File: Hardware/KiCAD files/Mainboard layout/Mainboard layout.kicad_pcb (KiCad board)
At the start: 2 copper layers, 174.5 x 169.2 mm, 67 parts, among them J1 MSD-1-A, J10 Conn_01x02, J11 Conn_01x04, J12 JST_06, J13 Conn_01x08, J17 PINHD_1x8_Male, J18 PINHD_1x8_Male, J19 PINHD_1x8_Male, J2 Screw_Terminal_2_P5.00mm, J20 PINHD_1x8_Male, J22 PINHD_1x8_Male, J23 PINHD_1x8_Male, J24 PINHD_1x8_Male, J25 Conn_01x04, J26 Conn_01x04, J27 Conn_01x04, J28 PINHD_1x8_Male, J3 Screw_Terminal_2_P3.50mm, J30 USB-A1VSB6, J31 JST_03, J34 JST_03, J35 JST_03, J36 JST_03, J37 JST_03, J38 JST_03, J4 JST_06, J5 Conn_01x04, J6 JST_06, J7 JST_06, J8 Conn_01x06, J9 Conn_01x10, Q1 BS170, Q2 2DD1664, SW8 Push_Button, SW9 Push_Button, U12 ESP32-S3-WROOM-1, U3 PCA9534PW, U5 PCA9534PW

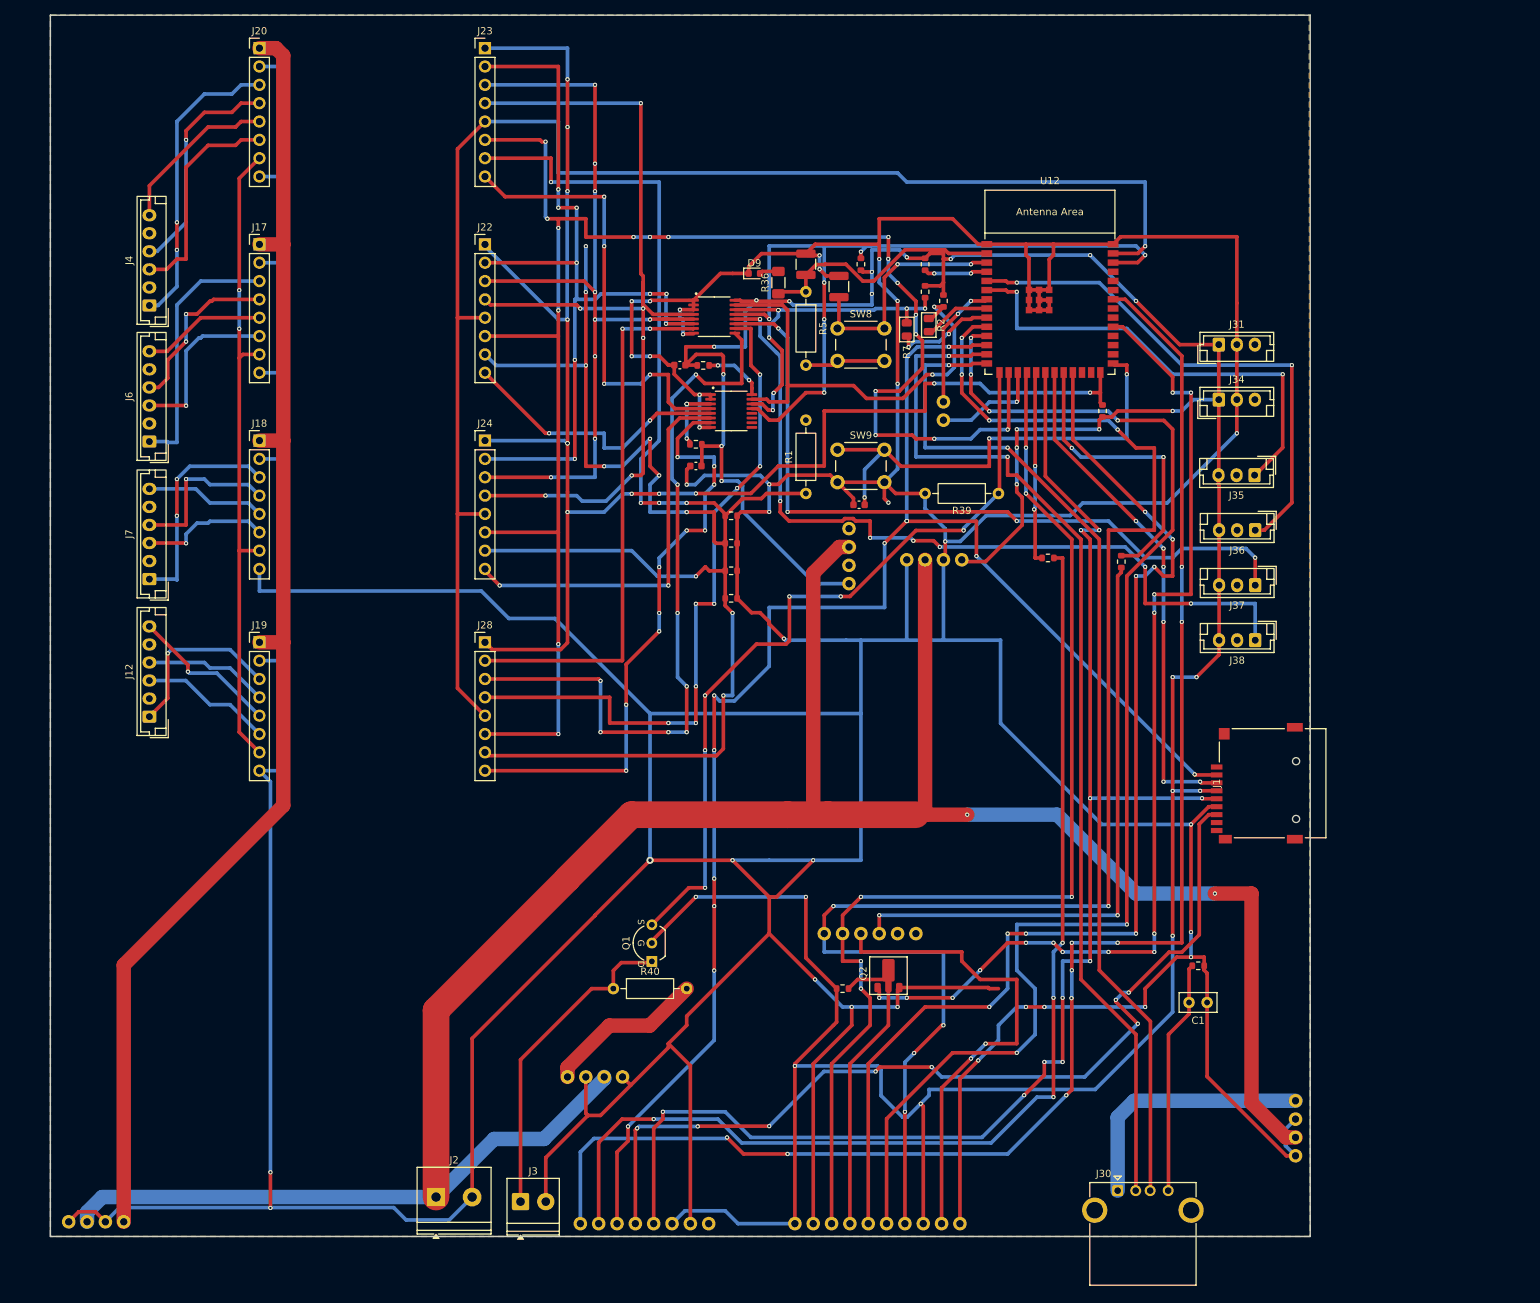
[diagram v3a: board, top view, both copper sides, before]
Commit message: general progress and adjustments
new footprint for pi reg inductor, var reg checked concurred with current part and value. re footprinted motor driver. started swapping head. adjusted some device footprints.
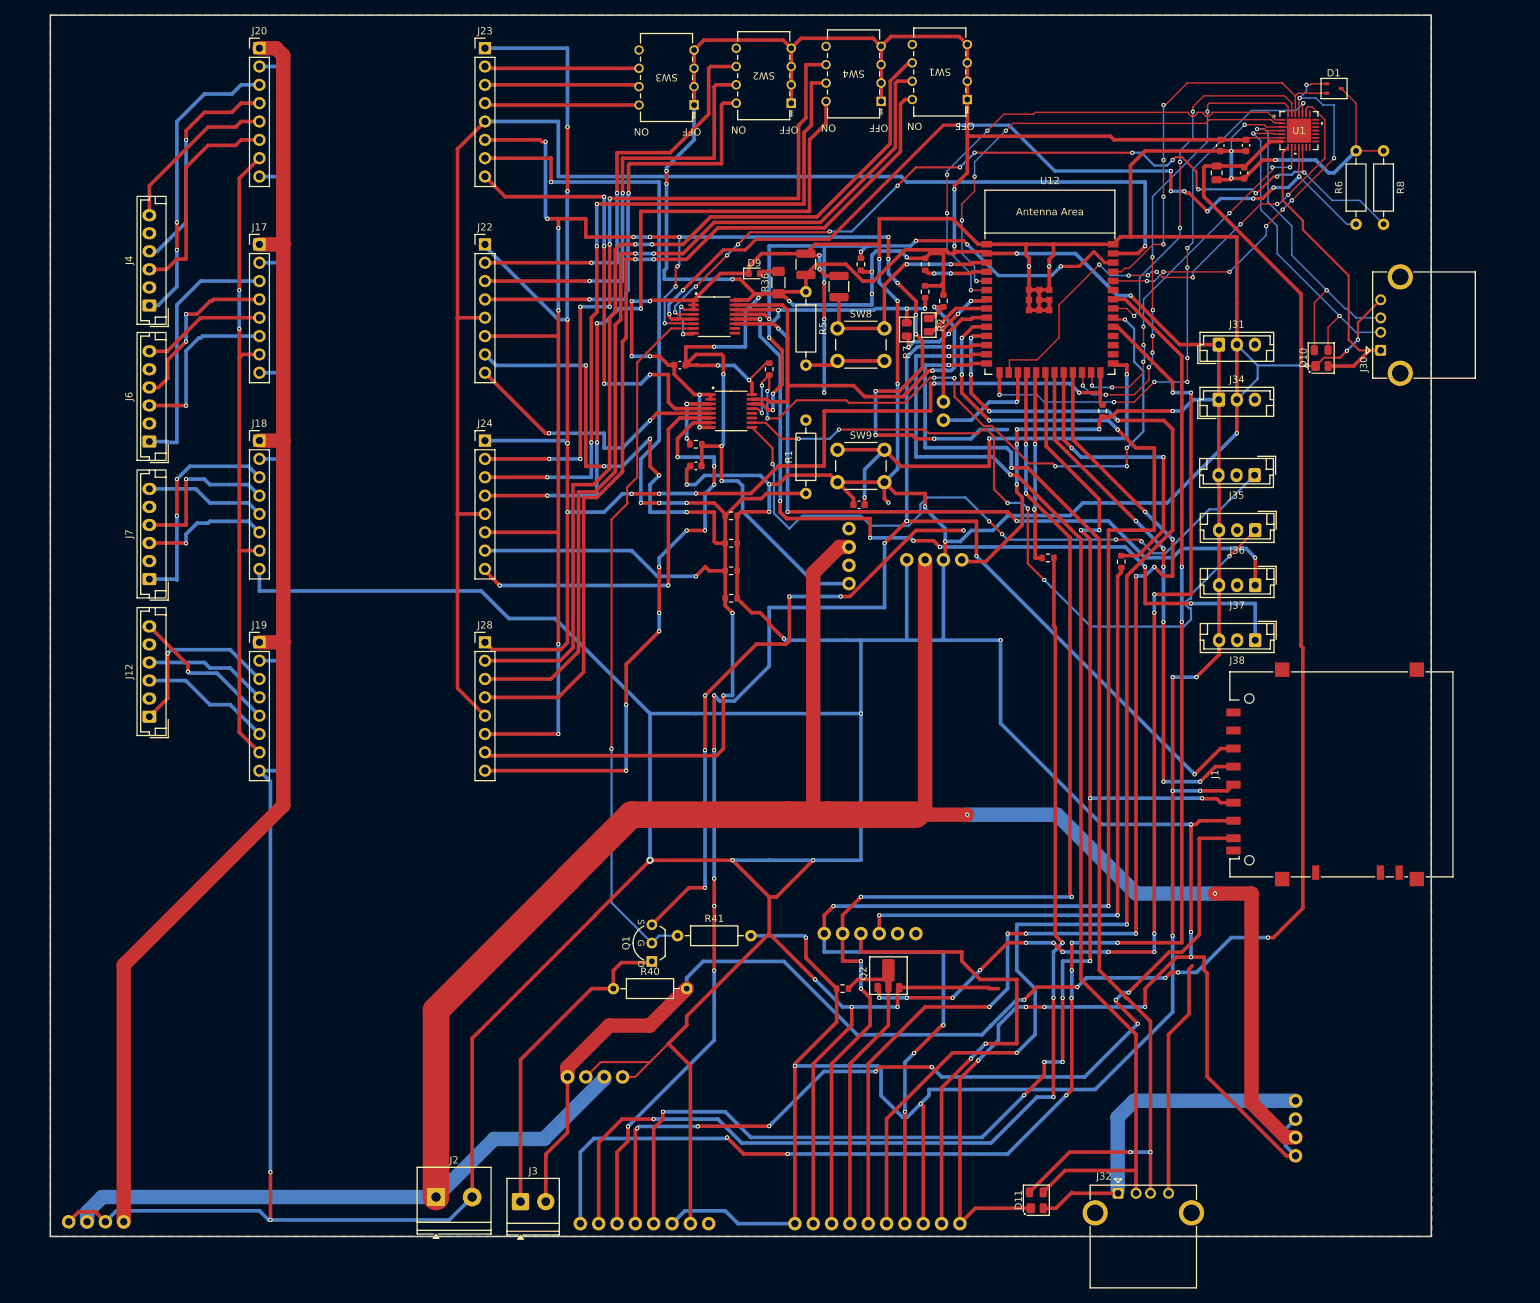
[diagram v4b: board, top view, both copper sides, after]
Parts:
- removed C1: 1nF_Ceramic, Capacitor_THT:C_Disc_D5.0mm_W2.5mm_P2.50mm
- removed R39: 10k, Resistor_THT:R_Axial_DIN0207_L6.3mm_D2.5mm_P10.16mm_Horizontal
- removed R54: 10k, PCM_SparkFun-Resistor:R_0603_1608Metric
- added C6: 0.1uF, PCM_SparkFun-Capacitor:C_0603_1608Metric, F.Cu at (200.7, 10.2)
- added C7: 0.1uF, PCM_SparkFun-Capacitor:C_0603_1608Metric, F.Cu at (200.4, 14.0)
- added C8: 1.0uF, PCM_SparkFun-Capacitor:C_0805_2012Metric, F.Cu at (196.6, 14.0)
- added C9: 4.7uF, PCM_SparkFun-Capacitor:C_0603_1608Metric, F.Cu at (197.1, 10.2)
- added D1: SP0502BAJT, PCM_Package_TO_SOT_SMD_AKL:SOT-323_SC-70, F.Cu at (212.9, 2.29)
- added D10: SP0503BAHT, PCM_Package_TO_SOT_SMD_AKL:SOT-143, F.Cu at (211.1, 39.6)
- added D11: SP0503BAHT, PCM_Package_TO_SOT_SMD_AKL:SOT-143, F.Cu at (171.6, 156.3)
- added J32: USB-A1VSB6, Connector_USB:USB_A_Kycon_KUSBX-AS1N-B_Horizontal, F.Cu at (182.9, 155.3)
- added R41: 10k, Resistor_THT:R_Axial_DIN0207_L6.3mm_D2.5mm_P10.16mm_Horizontal, F.Cu at (121.9, 119.6)
- added R57: 10k, PCM_SparkFun-Resistor:R_0603_1608Metric, F.Cu at (134.6, 41.1)
- added R8: 10k, Resistor_THT:R_Axial_DIN0207_L6.3mm_D2.5mm_P10.16mm_Horizontal, F.Cu at (219.7, 10.9)
- added SW1: 210-4MS, 4-pin DIP switch:DIP8_210-4_CTS, F.Cu at (162.1, 3.81)
- added SW2: 210-4MS, 4-pin DIP switch:DIP8_210-4_CTS, F.Cu at (137.7, 4.32)
- added SW3: 210-4MS, 4-pin DIP switch:DIP8_210-4_CTS, F.Cu at (124.2, 4.57)
- added SW4: 210-4MS, 4-pin DIP switch:DIP8_210-4_CTS, F.Cu at (150.1, 4.06)
- added U1: CP2102-GM, CP2102:QFN28_5X5_SIL, F.Cu at (208.0, 8.12)
- J1: footprint MMC_Footprints:CONN9_MSD-1_CUD -> Connector_Card:SD_Hirose_DM1AA_SF_PEJ82
- R40: value 100k -> 10k
- R6: value 1M -> 10k; footprint PCM_SparkFun-Resistor:R_0603_1608Metric -> Resistor_THT:R_Axial_DIN0207_L6.3mm_D2.5mm_P10.16mm_Horizontal
- moved J30 122.0 mm to (219.3, 38.6), turned to 90 degrees
- moved R6 105.0 mm to (215.9, 21.1), turned to 90 degrees
- moved J1 9.60 mm to (213.9, 97.3)
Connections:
- J22 pad 2: MODE_2_GPIO -> MODE_2_GPIO1
- J22 pad 3: MODE_1_GPIO -> MODE_1_GPIO1
- J22 pad 4: MODE_0_GPIO -> MODE_0_GPIO1
- J23 pad 2: MODE_2_GPIO -> MODE_2_GPIO0
- J23 pad 3: MODE_1_GPIO -> MODE_1_GPIO0
- J23 pad 4: MODE_0_GPIO -> MODE_0_GPIO0
- J24 pad 2: MODE_2_GPIO -> MODE_2_GPIO2
- J24 pad 3: MODE_1_GPIO -> MODE_1_GPIO2
- J24 pad 4: MODE_0_GPIO -> MODE_0_GPIO2
- J3 pad 2: GND -> +5V
- J30 pad 1: +5V_HIGHPW -> VBus
- J30 pad 2: D- -> Prog_D-
- J30 pad 3: D+ -> Prog_D+
- J30 pad 4: Net-(J30-GND) -> GND
- Q1 pad 2: +3.3V -> 3.3V_in1
- Q1 pad 3: 3.3V_in1 -> GND
- R55 pad 2: IO_Interupter -> IO_Interupter1
- R6 pad 1: GND -> *Suspend
- R6 pad 2: Net-(J30-GND) -> GND
- U12 pad 13: D- -> PI_D-
- U12 pad 14: D+ -> PI_D+
- U12 pad 15: 3.3V_in1 -> RTS
- U12 pad 16: nSLP -> CTS
- U12 pad 24: unconnected-(U12-GPIO47/SPICLK_P/SUBSPICLK_P_DIFF-Pad24) -> DTR
- U12 pad 25: unconnected-(U12-GPIO48/SPICLK_N/SUBSPICLK_N_DIFF-Pad25) -> RST
- U12 pad 32: unconnected-(U12-MTCK/GPIO39/CLK_OUT3/SUBSPICS1-Pad32) -> IO_Interupter2
- U12 pad 33: unconnected-(U12-MTDO/GPIO40/CLK_OUT2-Pad33) -> DSR
- U12 pad 36: /RX -> RX
- U12 pad 37: /TX -> TX
- U12 pad 38: IO_Interupter -> IO_Interupter1
- U12 pad 5: AXIS_Y_ENDSTOP -> RI
- U12 pad 6: AXIS_X_ENDSTOP -> DCD
- U3 pad 10: MODE_0_GPIOE -> unconnected-(U3-IO5-Pad10)
- U3 pad 13: IO_Interupter -> IO_Interupter1
- U3 pad 4: MODE_0_GPIO -> Suspend
- U3 pad 5: MODE_1_GPIO -> *Suspend
- U3 pad 6: MODE_2_GPIO -> nSLP
- U3 pad 7: MODE_2_GPIOE -> 3.3V_in1
- U3 pad 9: MODE_1_GPIOE -> unconnected-(U3-IO4-Pad9)
- U5 pad 10: unconnected-(U5-IO5-Pad10) -> AXIS_Y_ENDSTOP
- U5 pad 13: IO_Interupter -> IO_Interupter2
- U5 pad 16: Net-(U5-VDD) -> +3.3V
- U5 pad 9: unconnected-(U5-IO4-Pad9) -> AXIS_X_ENDSTOP
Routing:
- net +5V: track 22.4 -> 260.9 mm, vias 0 -> 5
- net GND: track 1227.7 -> 1450.9 mm, vias 35 -> 53
- net +3.3V: track 530.3 -> 697.6 mm, vias 26 -> 31
- net PI_D+: track 0.00 -> 162.9 mm, vias 0 -> 4
- net PI_D-: track 0.00 -> 158.9 mm, vias 0 -> 2
- net D-: track 146.3 -> 0.00 mm, vias 2 -> 0
- net D+: track 142.6 -> 0.00 mm, vias 2 -> 0
- net MODE_0_GPIO: track 129.8 -> 0.00 mm, vias 6 -> 0
- net *Suspend: track 0.00 -> 126.1 mm, vias 0 -> 10
- net Suspend: track 0.00 -> 122.8 mm, vias 0 -> 14
- net MODE_1_GPIO: track 114.4 -> 0.00 mm, vias 9 -> 0
- net MODE_2_GPIO: track 113.2 -> 0.00 mm, vias 9 -> 0
- net IO_Interupter: track 107.7 -> 0.00 mm, vias 6 -> 0
- net MODE_2_GPIO2: track 0.00 -> 101.3 mm, vias 0 -> 6
- net MODE_1_GPIO2: track 0.00 -> 100.8 mm, vias 0 -> 4
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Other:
- board size 174.5 x 169.2 mm -> 191.3 x 169.2 mm

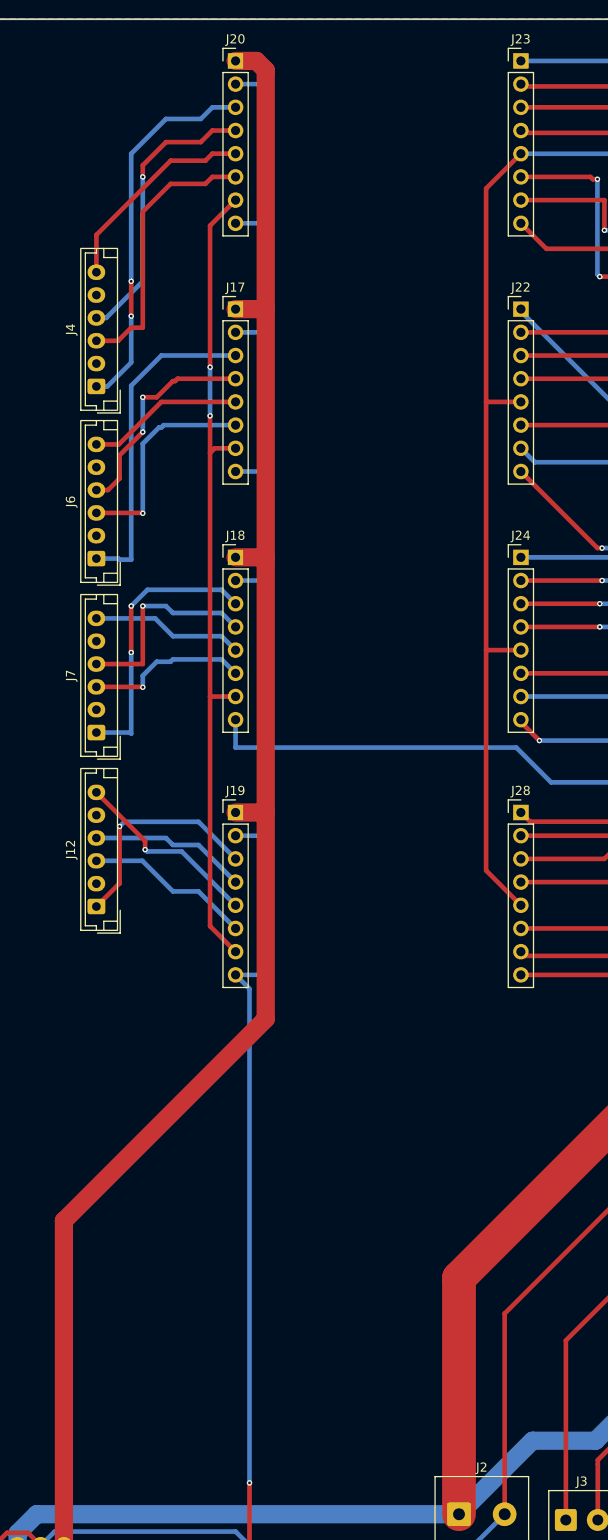
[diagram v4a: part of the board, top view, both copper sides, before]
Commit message: general updates to the schematics and layouts
includes some backchecks tot he master schematic to be accurate for the paper
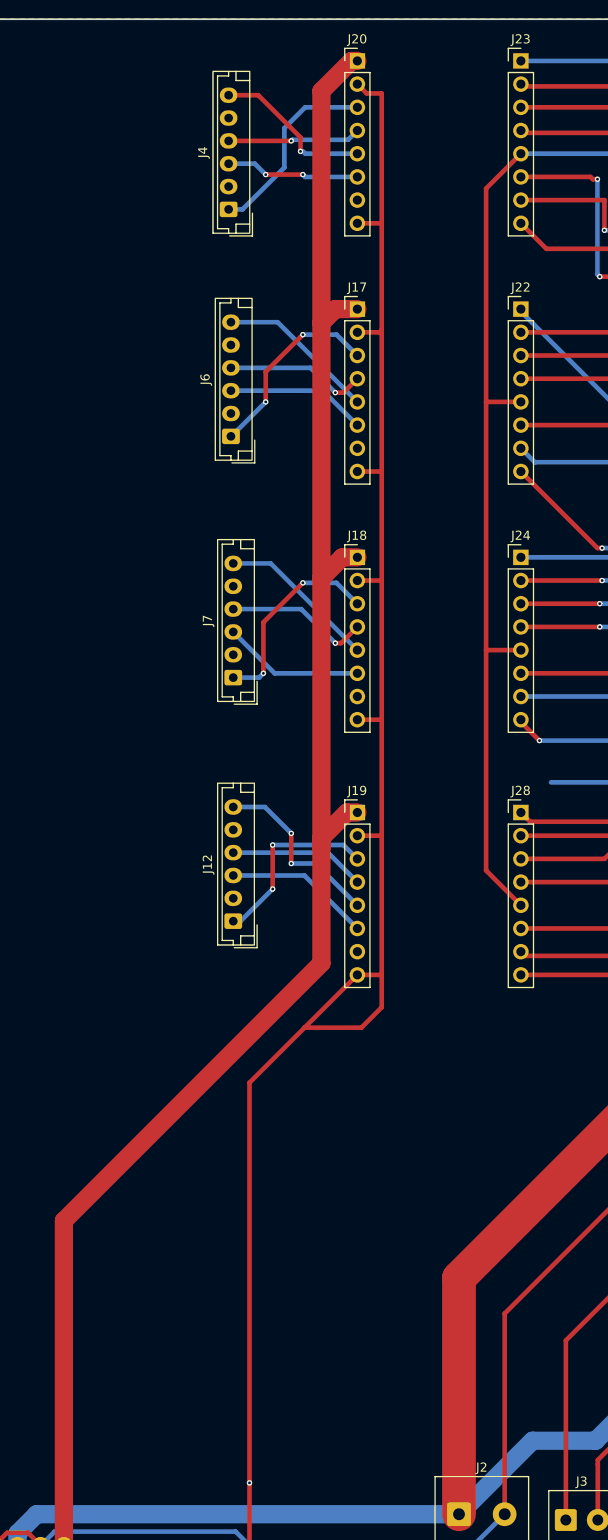
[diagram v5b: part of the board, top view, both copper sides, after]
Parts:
- moved J4 24.2 mm to (63.2, 13.0)
- moved J6 19.9 mm to (63.5, 37.8)
- moved J7 16.1 mm to (63.8, 64.2)
- moved J12 15.1 mm to (63.8, 90.9)
- moved J17 13.3 mm to (77.3, 23.9)
- moved J18 13.3 mm to (77.3, 51.1)
- moved J19 13.3 mm to (77.3, 79.0)
- moved J20 13.3 mm to (77.3, -3.30)
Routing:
- net nFault: track 90.4 -> 0.00 mm, vias 2 -> 0
- net GND: track 1450.9 -> 1425.6 mm
- net B2_DRV0: track 41.3 -> 21.3 mm, vias 2 -> 0
- net B1_DRV0: track 31.2 -> 14.6 mm
- net A2_DRV0: track 30.1 -> 14.7 mm, vias 0 -> 2
- net B2_DRV1: track 35.7 -> 21.3 mm, vias 0 -> 2
- net B2_DRV2: track 30.6 -> 22.1 mm
- net B1_DRV1: track 24.0 -> 15.6 mm, vias 2 -> 1
- net A2_DRV1: track 23.7 -> 15.4 mm, vias 1 -> 0
- net +12V: track 184.3 -> 191.8 mm
- net B1_DRV2: track 22.5 -> 15.9 mm
- net A1_DRV0: track 23.0 -> 17.6 mm, vias 0 -> 1
- net B2_DRVE: track 24.4 -> 20.5 mm, vias 1 -> 2
- net A2_DRV2: track 17.9 -> 15.5 mm, vias 1 -> 0
- net A2_DRVE: track 18.3 -> 16.0 mm
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
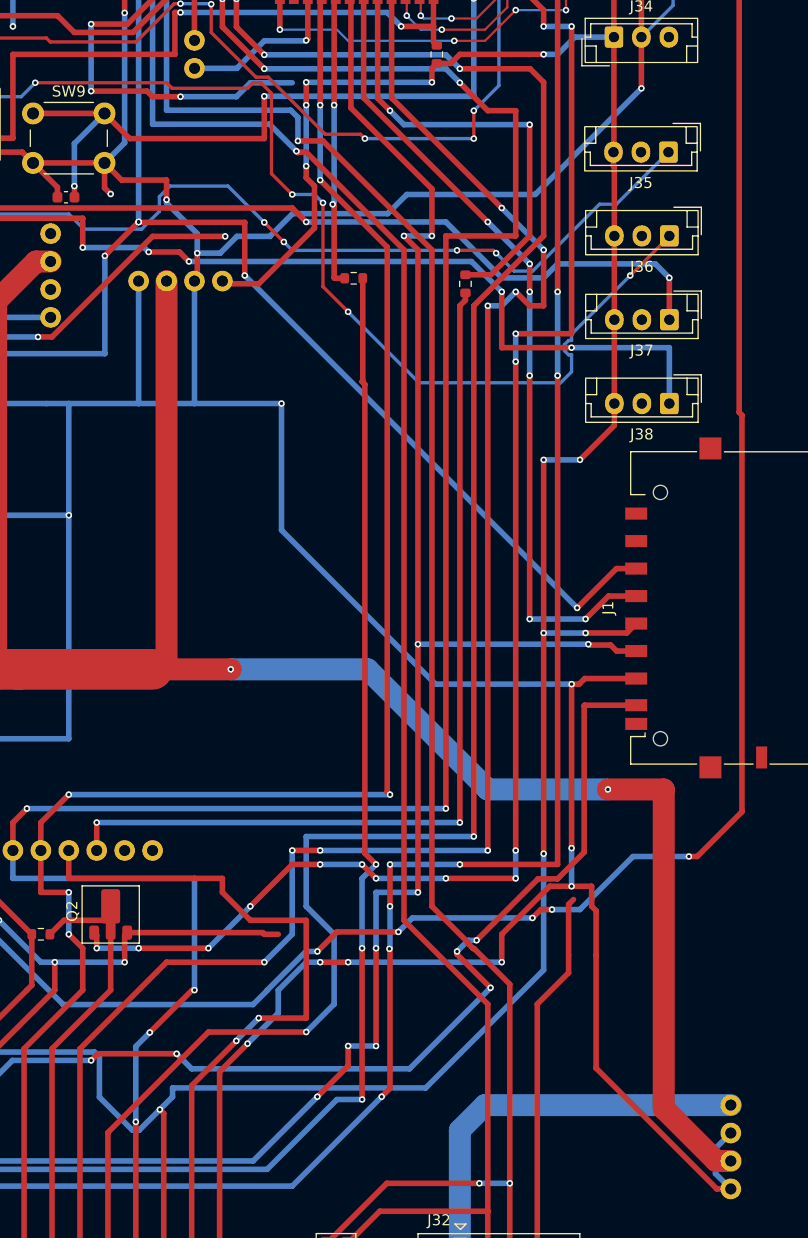
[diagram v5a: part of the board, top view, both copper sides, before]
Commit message: DRV 8825 and regulator purchased set
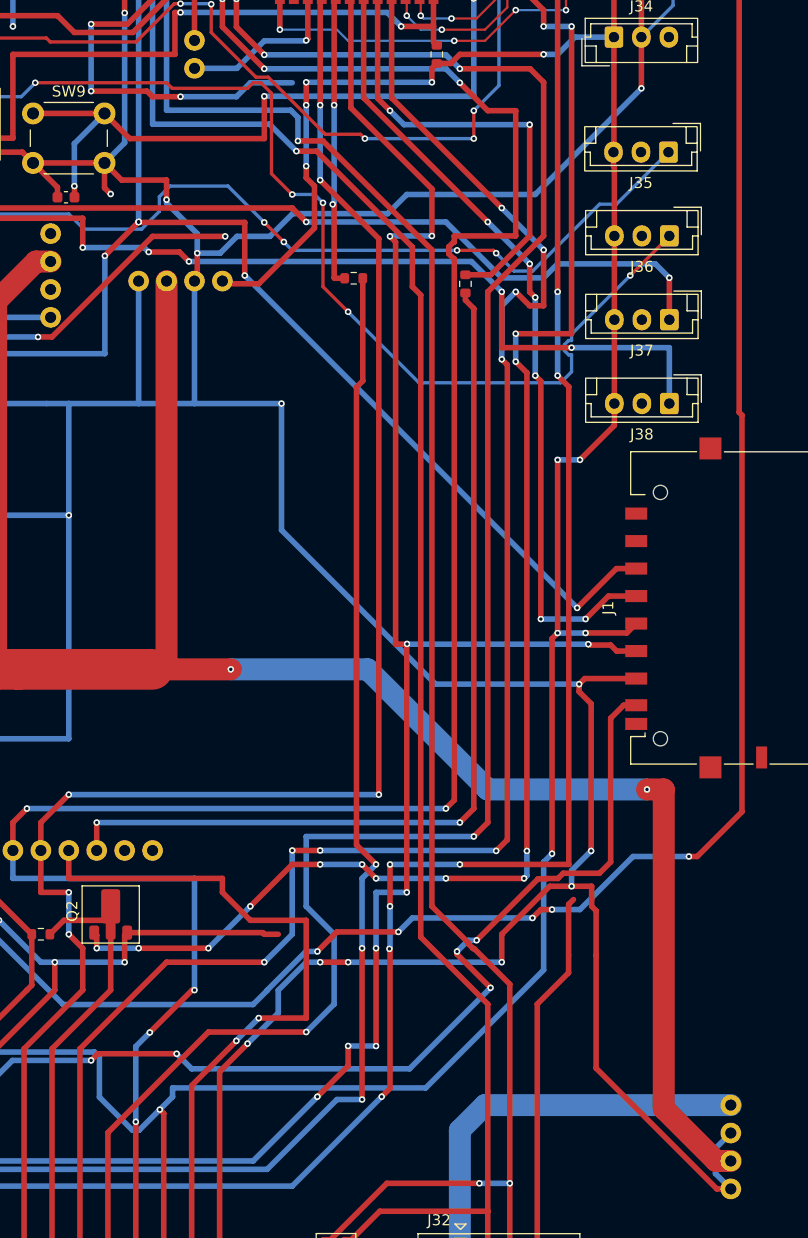
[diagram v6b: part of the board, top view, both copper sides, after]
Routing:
- net +3.3V: track 697.6 -> 695.6 mm
- net SPI1_CLK: track 203.8 -> 205.8 mm
- net SPI4_CS: track 155.9 -> 154.5 mm
- net DRDY_ALOW: track 213.1 -> 214.6 mm
- net Net-(Q2-B): track 141.3 -> 142.6 mm
- net GND: track 1425.6 -> 1426.8 mm
- net MISO_4: track 83.9 -> 84.6 mm
- net MOSI_1: track 73.5 -> 72.9 mm
- net PI_D-: track 158.9 -> 159.5 mm
